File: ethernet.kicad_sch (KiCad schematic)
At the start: 45 parts

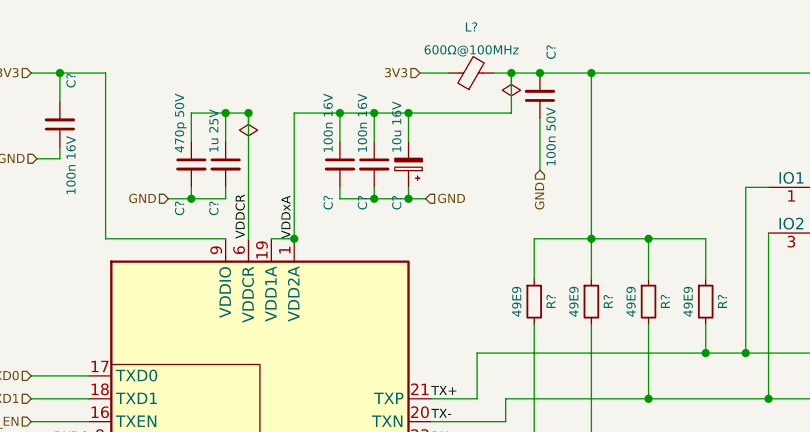
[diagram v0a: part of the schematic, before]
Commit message: #4 Wrong polarity on C207
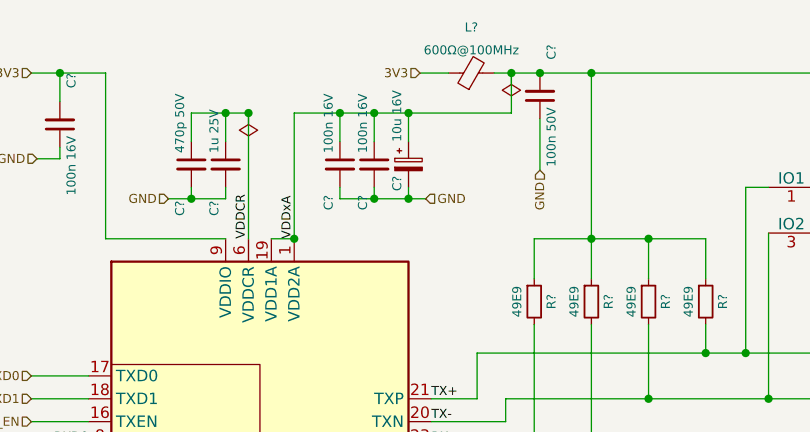
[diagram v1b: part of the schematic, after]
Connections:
- net GND: now also C?.2; no longer C?.1
- net VDDxA: now also C?.1; no longer C?.2
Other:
- moved on the sheet: C?
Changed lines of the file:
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@@
     )
   )
-  (symbol (lib_id "Device:C_Polarized_Small") (at 112.395 42.545 180) (unit 1)
+  (symbol (lib_id "Device:C_Polarized_Small") (at 112.395 42.545 0) (unit 1)
     (in_bom yes) (on_board yes) (dnp no)
-    (property "Reference" "C?" (at 111.125 47.625 90)
+    (property "Reference" "C?" (at 111.125 43.815 90)
       (effects (font (size 1 1)) (justify right))
     )
-    (property "Value" "10u 16V" (at 111.125 41.275 90)
+    (property "Value" "10u 16V" (at 111.125 34.29 90)
       (effects (font (size 1 1)) (justify right))
     )
